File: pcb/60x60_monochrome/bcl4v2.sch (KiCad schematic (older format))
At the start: 51 parts, among them J1 Conn_01x05, J10 Conn_01x01_Female, J11 Conn_01x01_Female, J12 Conn_01x01_Female, J13 Conn_01x01_Female, J14 Conn_01x02, J15 Conn_01x04, J2 Conn_01x05, J3 USB_OTG, J4 Conn_01x05, J5 Conn_01x05, J6 Conn_01x05, J7 Conn_01x05, J8 Conn_01x05, J9 Conn_01x05, SW1 SW_Push, SW2 SW_Push, U1 DS9166A-23, U2 STM32F070CBTx, U3 NPIC6C595, U4 M54564FP, Y1 Resonator

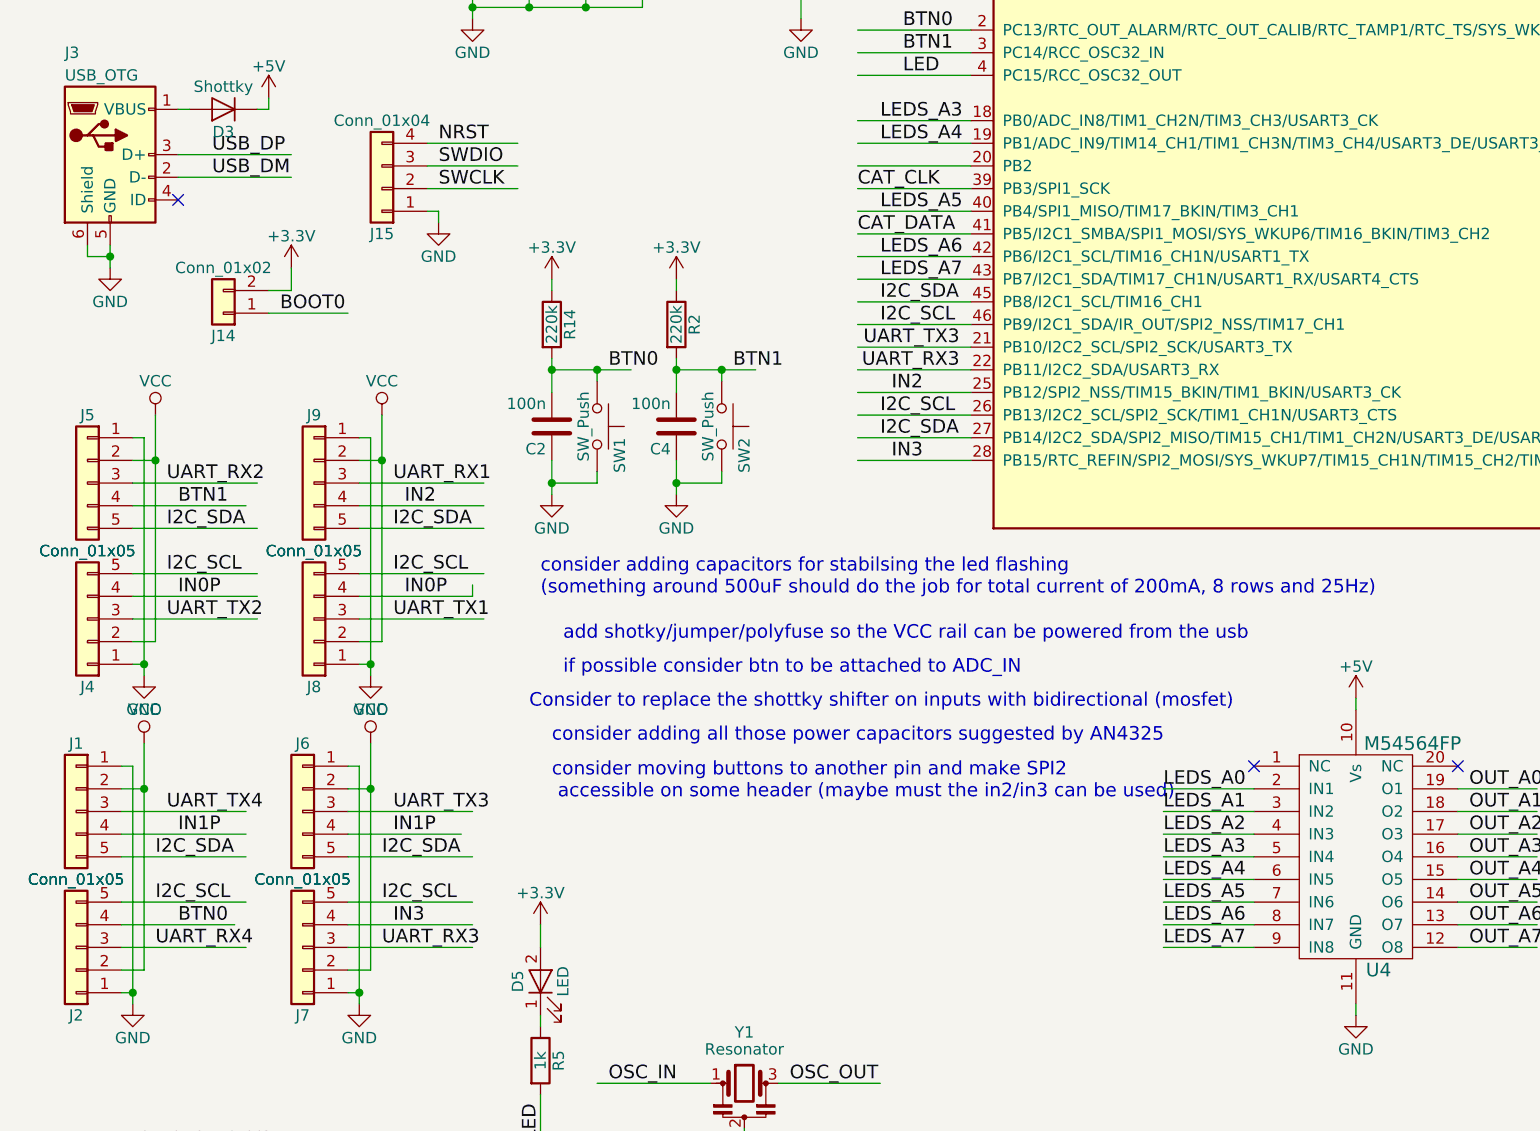
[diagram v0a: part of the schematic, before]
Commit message: - make the headers better solderable
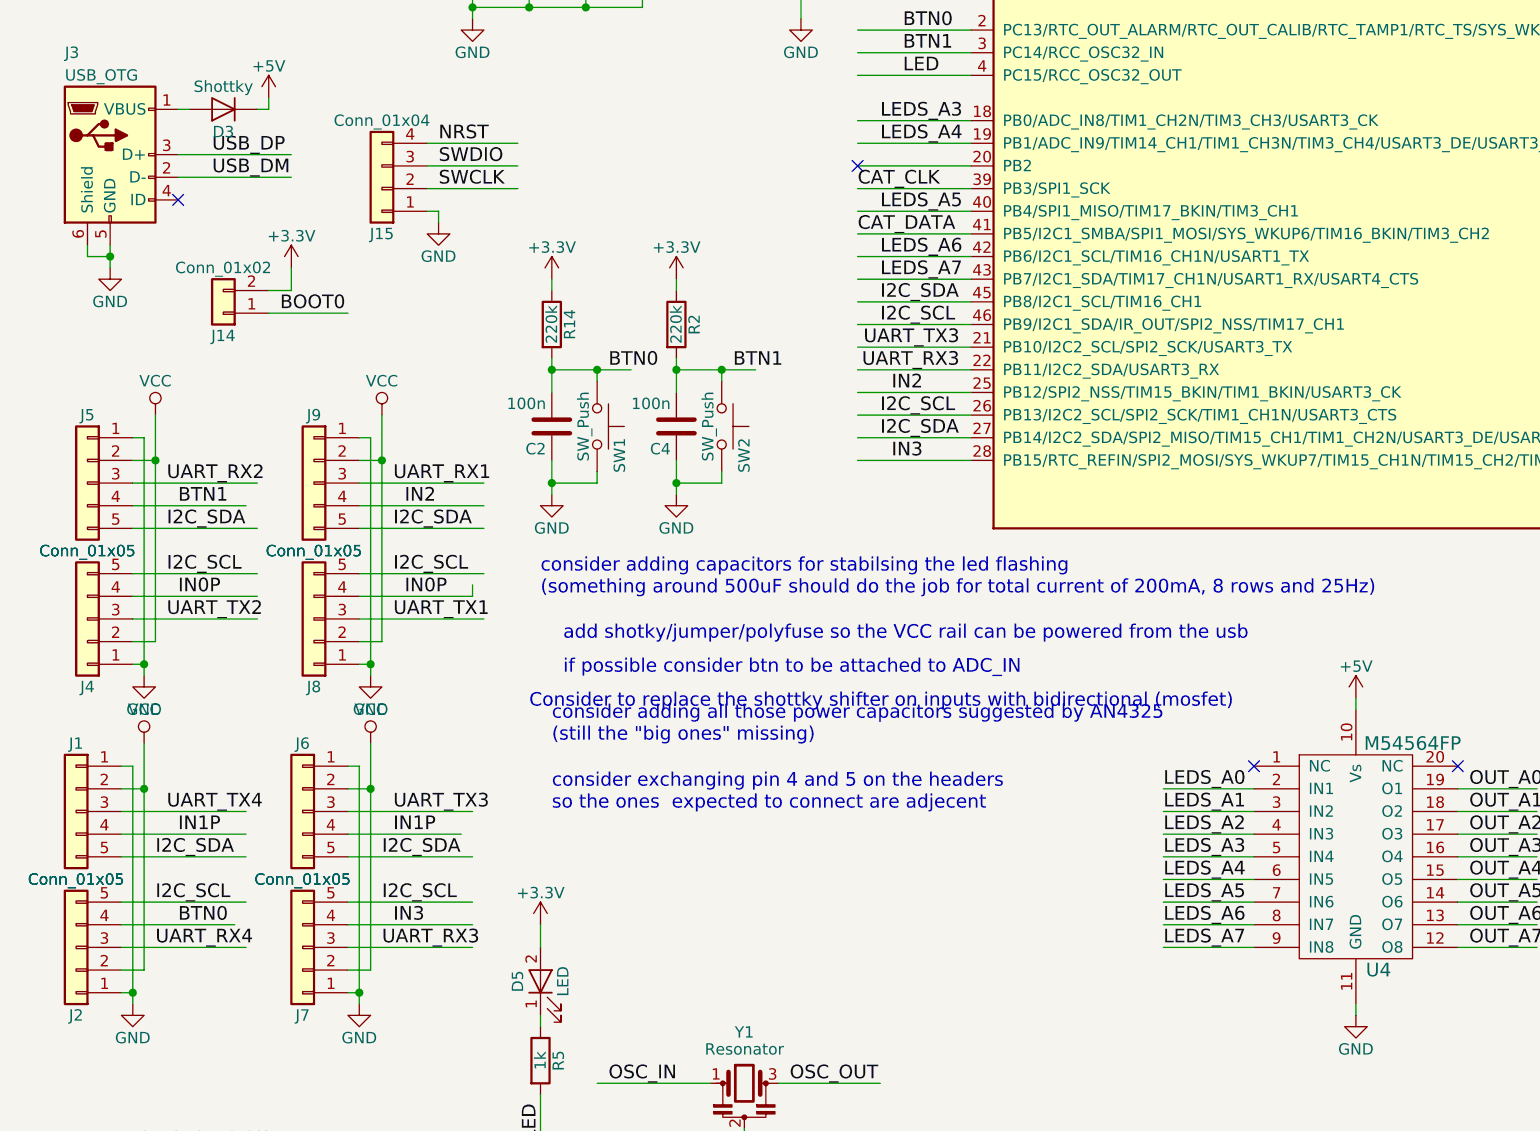
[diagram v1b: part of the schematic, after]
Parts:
- J14: footprint Pin_Headers:Pin_Header_Angled_1x02_Pitch2.54mm -> kicad_libraries_new:badger_Pin_Hdr_1x02_2.54mm_angled_handsolder
- J15: footprint Pin_Headers:Pin_Header_Angled_1x04_Pitch2.54mm -> kicad_libraries_new:badger_Pin_Hdr_1x04_2.54mm_angled_handsolder
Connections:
- no-connect marks 8 -> 9
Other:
- note added: "consider adding all those power capacitors suggested by AN4325\n(still the "big ones" missing)"
- note added: "consider exchanging pin 4 and 5 on the headers\nso the ones expected to connect are adjecent"
- note removed: "consider adding all those power capacitors suggested by AN4325"
- note removed: "consider moving buttons to another pin and make SPI2\n accessible on some header (maybe must the in2/in3 can be used)"
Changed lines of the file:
@@
 LIBS:badger_m54564fp
 LIBS:badger_npic6c595
+LIBS:bcl4v2-cache
 EELAYER 25 0
 EELAYER END
@@
 F 0 "J14" H 1250 3150 50  0000 C CNN
 F 1 "Conn_01x02" H 1250 2850 50  0000 C CNN
-F 2 "Pin_Headers:Pin_Header_Angled_1x02_Pitch2.54mm" H 1250 3050 50  0001 C CNN
+F 2 "kicad_libraries_new:badger_Pin_Hdr_1x02_2.54mm_angled_handsolder" H 1250 3050 50  0001 C CNN
 F 3 "" H 1250 3050 50  0001 C CNN
 	1    1250 3050
@@
 F 0 "J15" H 1950 2700 50  0000 C CNN
 F 1 "Conn_01x04" H 1950 2200 50  0000 C CNN
-F 2 "Pin_Headers:Pin_Header_Angled_1x04_Pitch2.54mm" H 1950 2500 50  0001 C CNN
+F 2 "kicad_libraries_new:badger_Pin_Hdr_1x04_2.54mm_angled_handsolder" H 1950 2500 50  0001 C CNN
 F 3 "" H 1950 2500 50  0001 C CNN
 	1    1950 2500
@@
 Connection ~ 900  4600
 Wire Wire Line
-	850  4500 950  4500
-Wire Wire Line
-	950  4500 950  3500
+	950  4500 850  4500
+Wire Wire Line
+	950  3500 950  4500
 Wire Wire Line
 	850  3700 950  3700
@@
 Connection ~ 1900 4600
 Wire Wire Line
-	1850 4500 1950 4500
-Wire Wire Line
-	1950 4500 1950 3500
+	1950 4500 1850 4500
+Wire Wire Line
+	1950 3500 1950 4500
 Wire Wire Line
 	1850 3700 1950 3700
@@
 Connection ~ 850  6050
 Wire Wire Line
-	800  5950 900  5950
-Wire Wire Line
-	900  5950 900  4950
+	900  5950 800  5950
+Wire Wire Line
+	900  4950 900  5950
 Wire Wire Line
 	800  5150 900  5150
@@
 Connection ~ 1850 6050
 Wire Wire Line
-	1800 5950 1900 5950
-Wire Wire Line
-	1900 5950 1900 4950
+	1900 5950 1800 5950
+Wire Wire Line
+	1900 4950 1900 5950
 Wire Wire Line
 	1800 5150 1900 5150
@@
 	3650 1100 3650 1200
 Text Notes 2700 4950 0    60   ~ 0
-consider adding all those power capacitors suggested by AN4325
+consider adding all those power capacitors suggested by AN4325\n(still the "big ones" missing)
 $Comp
 L GND #PWR018
@@
 	1    0    0    -1
 $EndComp
-Text Notes 2700 5200 0    60   ~ 0
-consider moving buttons to another pin and make SPI2\n accessible on some header (maybe must the in2/in3 can be used)
 $Comp
 L C C6
@@
 	1    0    0    -1
 $EndComp
+Text Notes 2700 5250 0    60   ~ 0
+consider exchanging pin 4 and 5 on the headers\nso the ones  expected to connect are adjecent
+NoConn ~ 4050 2400
 $EndSCHEMATC

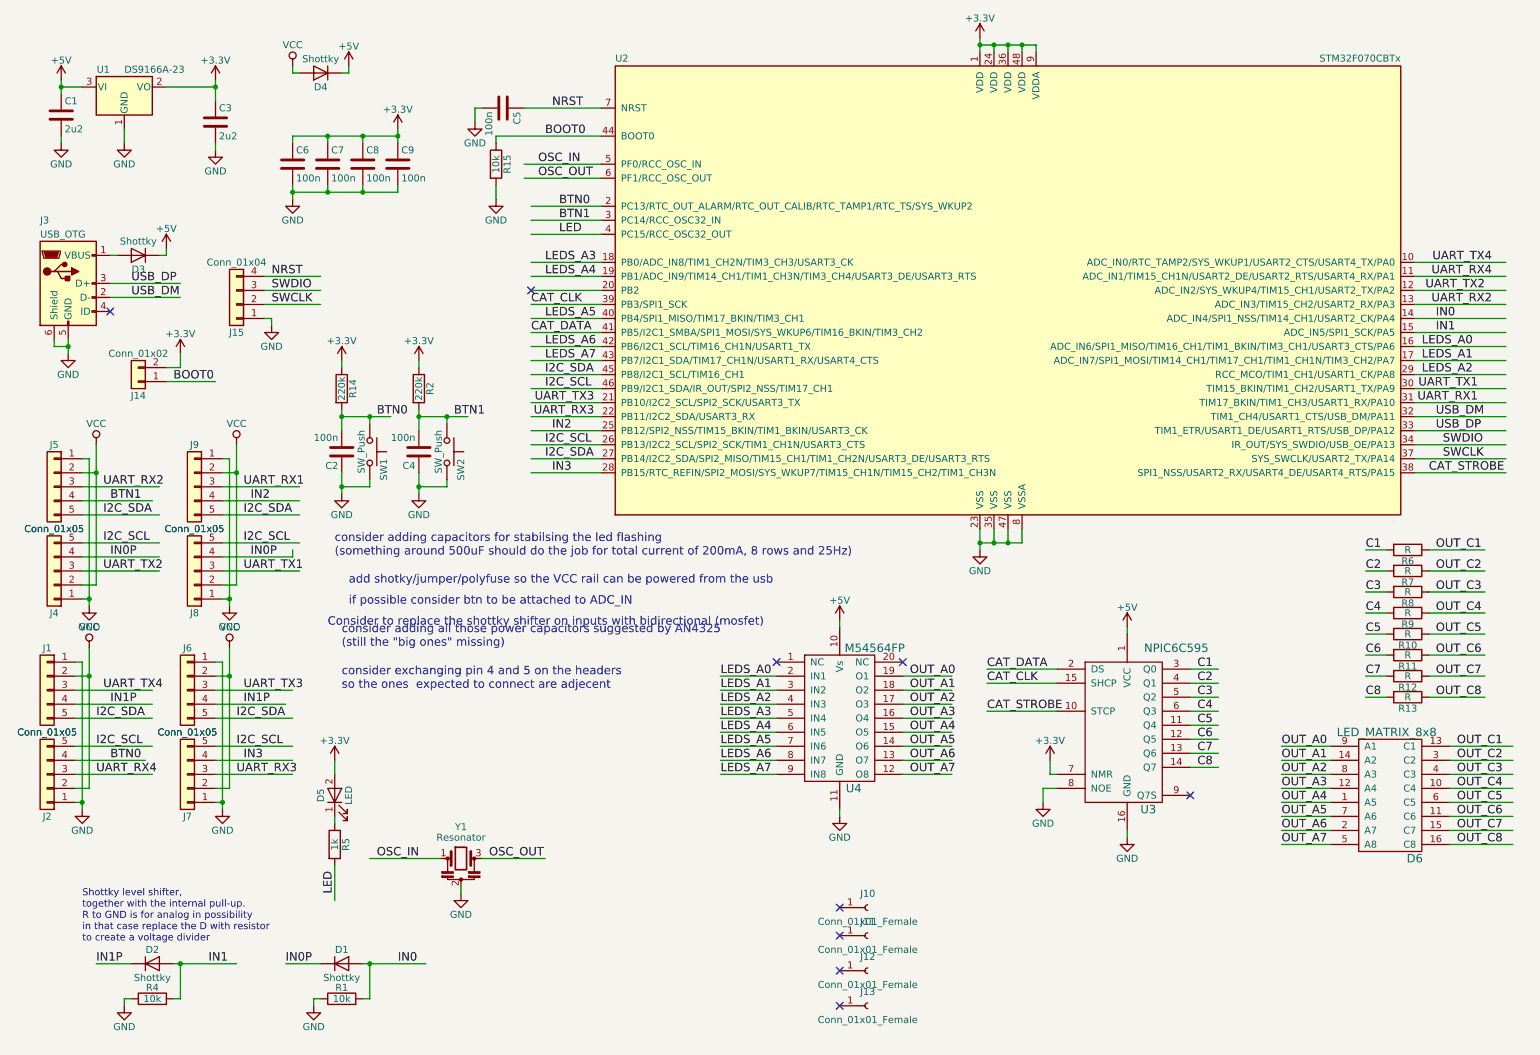
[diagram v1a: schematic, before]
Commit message: - split schematics to more pages
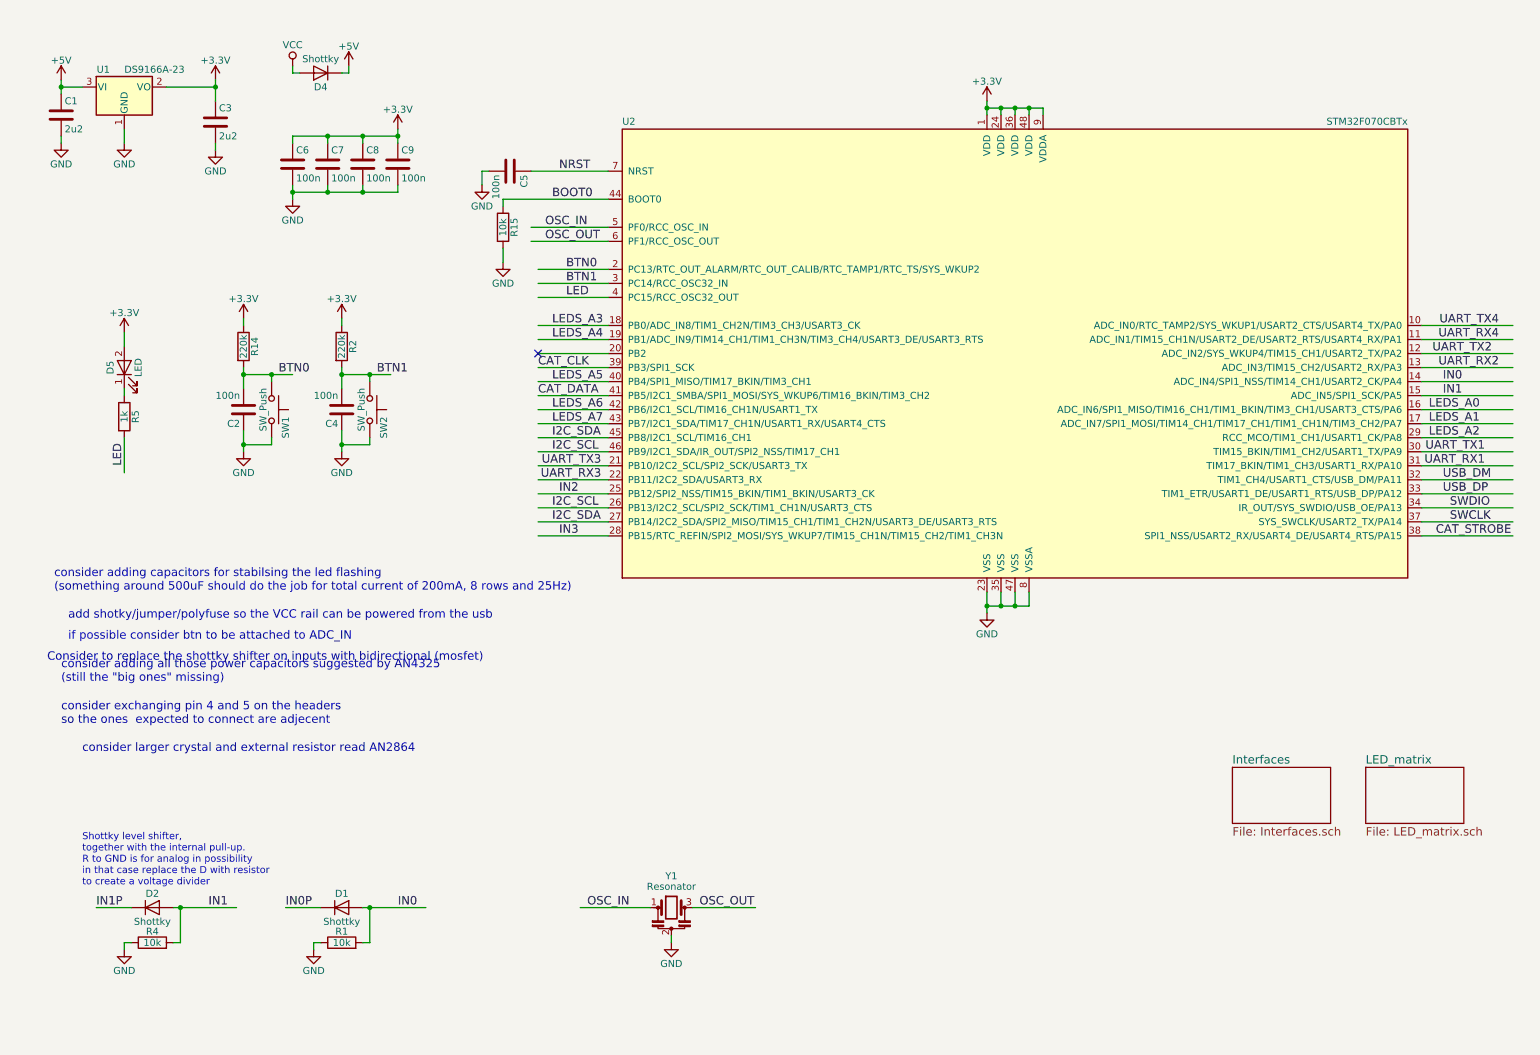
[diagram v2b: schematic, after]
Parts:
- removed D3: Shottky, Diodes_SMD:D_SOD-123, symbol D
- removed D6: LED_MATRIX_8x8, kicad_libraries_new:badger_LED_MATRIX_8x8_60.2mmx60.2mm, symbol LED_MATRIX_8x8
- removed J1, J2, J4, J5, J6, J7, J8, J9: Conn_01x05, kicad_libraries_new:badger_Pin_Hdr_1x05_2.54mm_handsolder, symbol Conn_01x05
- removed J10, J11, J12, J13: Conn_01x01_Female, badger_footprints_kicad_4x:badger_mount_M3, symbol Conn_01x01_Female
- removed J14: Conn_01x02, kicad_libraries_new:badger_Pin_Hdr_1x02_2.54mm_angled_handsolder, symbol Conn_01x02
- removed J15: Conn_01x04, kicad_libraries_new:badger_Pin_Hdr_1x04_2.54mm_angled_handsolder, symbol Conn_01x04
- removed J3: USB_OTG, Connect:USB_Micro-B, symbol USB_OTG
- removed R10, R11, R12, R13, R6, R7, R8, R9: R, Resistors_SMD:R_0805_HandSoldering, symbol R
- removed U3: NPIC6C595, Housings_SOIC:SOIC-16_3.9x9.9mm_Pitch1.27mm, symbol NPIC6C595
- removed U4: M54564FP, kicad_libraries_new:badger_20P2N_5.4x12.8mm_Pitch1.27mm, symbol M54564FP
- C6: Price (none) -> 4
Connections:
- net labels removed: C1, C2, C3, C4, C5, C6, C7, C8, OUT_A0, OUT_A1, OUT_A2, OUT_A3, OUT_A4, OUT_A5, OUT_A6, OUT_A7, OUT_C1, OUT_C2, OUT_C3, OUT_C4, OUT_C5, OUT_C6, OUT_C7, OUT_C8
- wire segments 239 -> 107
- no-connect marks 9 -> 1
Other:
- note added: "consider larger crystal and external resistor read AN2864"
- moved on the sheet: C2, C4, C5, D1, D2, D5, R1, R14, R15, R2, R4, R5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

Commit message: - add pins to the sheets, add reset/boot circuit
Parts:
- removed C5: 100n, Capacitors_SMD:C_0805_HandSoldering, symbol C
- removed R15: 10k, Resistors_SMD:R_0805_HandSoldering, symbol R
- added C10: 4u7, Capacitors_SMD:C_0805_HandSoldering, symbol C
- added C11: 100n, Capacitors_SMD:C_0805_HandSoldering, symbol C
- added C12, C13: 220u, Capacitors_Tantalum_SMD:CP_Tantalum_Case-V_EIA-7343-20_Hand, symbol CP
- added Q1: BSS138, kicad_libraries_new:badger_SOT-23_handsolder, symbol BSS138
- added R13: 10k, Resistors_SMD:R_0805_HandSoldering, symbol R
- added R16: 820k, Resistors_SMD:R_0805_HandSoldering, symbol R
- added SW3: SW_Push, kicad_libraries_new:badger_smd_button_KSS231G, symbol SW_Push
- C1, C3: value 2u2 -> 4u7
- D1, D2, D4: footprint LEDs:LED_0805_HandSoldering -> kicad_libraries_new:badger_D_SOD-123_hand
- R1, R4: footprint Capacitors_SMD:C_0805_HandSoldering -> Resistors_SMD:R_0805_HandSoldering
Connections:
- wire segments 107 -> 157
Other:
- note added: "Add hierarchical pins to LED_matrix sheet"
- note added: "C12,C13 are only for stability if the power supply is not stable enough"
- note added: "Either Q1,SW3,C10, C11, R13, R16 or \nC11 and R13 in place of C10 (and eventually J13)"
- note added: "Reset <1s\nbootloader > 3s"
- note removed: "consider adding capacitors for stabilsing the led flashing\n(something around 500uF should do the job for total current of 200mA, 8 rows and 25Hz)"
- note removed: "consider exchanging pin 4 and 5 on the headers\nso the ones expected to connect are adjecent"
- note removed: "if possible consider btn to be attached to ADC_IN\n"
- moved on the sheet: C2, C4, C6, C7, C8, C9, D1, D2, D4, D5, R1, R14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
